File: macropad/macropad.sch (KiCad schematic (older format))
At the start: 0 parts

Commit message: added new component lib
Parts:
- added C1, C2: 20p, symbol Device:C_Small
- added R1: 10K, symbol Device:R
- added SW1: RESET, symbol keyboard_parts:SW_PUSH
- added SW2: BOOT, symbol keyboard_parts:SW_PUSH
- added U1: ATmega328-PU, Package_DIP:DIP-28_W7.62mm, symbol MCU_Microchip_ATmega:ATmega328-PU
- added Y1: 16MHz, symbol Device:Crystal
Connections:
- new net: R1.2, SW1.1, U1.1 (~RESET~/PC6)
- new net: C1.1, U1.10 (XTAL2/PB7), Y1.2
- new net: SW2.1, U1.11 (PD5)
- new net: C2.1, U1.9 (XTAL1/PB6), Y1.1
- new net +5V: C1.2, C2.2, SW1.2, SW2.2, U1.22 (GND), U1.8 (GND)
- new net VCC: R1.1, U1.20 (AVCC), U1.7 (VCC)
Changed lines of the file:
@@
 EESchema Schematic File Version 4
+LIBS:macropad-cache
 EELAYER 26 0
 EELAYER END
@@
 Comment4 ""
 $EndDescr
+$Comp
+L MCU_Microchip_ATmega:ATmega328-PU U1
+U 1 1 5CCD0C9A
+P 2200 5200
+F 0 "U1" H 1559 5246 50  0000 R CNN
+F 1 "ATmega328-PU" H 1559 5155 50  0000 R CNN
+F 2 "Package_DIP:DIP-28_W7.62mm" H 2200 5200 50  0001 C CIN
+F 3 "http://ww1.microchip.com/downloads/en/DeviceDoc/ATmega328_P%20AVR%20MCU%20with%20picoPower%20Technology%20Data%20Sheet%2040001984A.pdf" H 2200 5200 50  0001 C CNN
+	1    2200 5200
+	1    0    0    -1
+$EndComp
+$Comp
+L Device:Crystal Y1
+U 1 1 5CCD0E54
+P 3950 4450
+F 0 "Y1" V 3904 4581 50  0000 L CNN
+F 1 "16MHz" V 3995 4581 50  0000 L CNN
+F 2 "" H 3950 4450 50  0001 C CNN
+F 3 "~" H 3950 4450 50  0001 C CNN
+F 4 " X176-ND " H 3950 4450 50  0001 C CNN "DPN"
+F 5 " ECS-160-20-4 " H 3950 4450 50  0001 C CNN "MPN"
+	1    3950 4450
+	0    1    1    0
+$EndComp
+Wire Wire Line
+	2800 4600 3650 4600
+Wire Wire Line
+	3650 4600 3650 4200
+Wire Wire Line
+	3650 4200 3950 4200
+Wire Wire Line
+	3950 4200 3950 4300
+Wire Wire Line
+	2800 4700 3950 4700
+Wire Wire Line
+	3950 4700 3950 4600
+$Comp
+L Device:C_Small C2
+U 1 1 5CCD1142
+P 4250 4900
+F 0 "C2" H 4342 4946 50  0000 L CNN
+F 1 "20p" H 4342 4855 50  0000 L CNN
+F 2 "" H 4250 4900 50  0001 C CNN
+F 3 "~" H 4250 4900 50  0001 C CNN
+F 4 "478-7724-ND" H 4250 4900 50  0001 C CNN "DPN"
+F 5 "SR151A200JAR" H 4250 4900 50  0001 C CNN "MPN"
+	1    4250 4900
+	1    0    0    -1
+$EndComp
+$Comp
+L Device:C_Small C1
+U 1 1 5CCD117E
+P 3950 4900
+F 0 "C1" H 4042 4946 50  0000 L CNN
+F 1 "20p" H 4042 4855 50  0000 L CNN
+F 2 "" H 3950 4900 50  0001 C CNN
+F 3 "~" H 3950 4900 50  0001 C CNN
+F 4 "SR151A200JAR" H 3950 4900 50  0001 C CNN "MPN"
+F 5 "478-7724-ND" H 3950 4900 50  0001 C CNN "DPN"
+	1    3950 4900
+	1    0    0    -1
+$EndComp
+Wire Wire Line
+	3950 4800 3950 4700
+Connection ~ 3950 4700
+Wire Wire Line
+	4250 4800 4250 4200
+Wire Wire Line
+	4250 4200 3950 4200
+Connection ~ 3950 4200
+$Comp
+L keyboard_parts:GND #PWR?
+U 1 1 5CCD12BD
+P 4250 5250
+F 0 "#PWR?" H 4250 5300 20  0001 C CNN
+F 1 "GND" H 4250 5309 30  0000 C CNN
+F 2 "" H 4250 5250 60  0000 C CNN
+F 3 "" H 4250 5250 60  0000 C CNN
+	1    4250 5250
+	1    0    0    -1
+$EndComp
+Wire Wire Line
+	4250 5000 4250 5100
+Wire Wire Line
+	3950 5000 3950 5100
+Wire Wire Line
+	3950 5100 4250 5100
+Connection ~ 4250 5100
+Wire Wire Line
+	4250 5100 4250 5250
+$Comp
+L power:VCC #PWR?
+U 1 1 5CCD1372
+P 2200 3300
+F 0 "#PWR?" H 2200 3150 50  0001 C CNN
+F 1 "VCC" H 2217 3473 50  0000 C CNN
+F 2 "" H 2200 3300 50  0001 C CNN
+F 3 "" H 2200 3300 50  0001 C CNN
+	1    2200 3300
+	1    0    0    -1
+$EndComp
+Wire Wire Line
+	2200 3700 2200 3450
+Wire Wire Line
+	2300 3700 2300 3450
+Wire Wire Line
+	2300 3450 2200 3450
+Connection ~ 2200 3450
+Wire Wire Line
+	2200 3450 2200 3300
+$Comp
+L keyboard_parts:GND #PWR?
+U 1 1 5CCD165F
+P 2200 6950
+F 0 "#PWR?" H 2200 7000 20  0001 C CNN
+F 1 "GND" H 2200 7009 30  0000 C CNN
+F 2 "" H 2200 6950 60  0000 C CNN
+F 3 "" H 2200 6950 60  0000 C CNN
+	1    2200 6950
+	1    0    0    -1
+$EndComp
+Wire Wire Line
+	2200 6700 2200 6950
+$Comp
+L keyboard_parts:SW_PUSH SW1
+U 1 1 5CCD150D
+P 3950 5700
+F 0 "SW1" H 3950 5955 50  0000 C CNN
+F 1 "RESET" H 3950 5864 50  0000 C CNN
+F 2 "" H 3950 5700 60  0000 C CNN
+F 3 "" H 3950 5700 60  0000 C CNN
+	1    3950 5700
+	1    0    0    -1
+$EndComp
+$Comp
+L keyboard_parts:SW_PUSH SW2
+U 1 1 5CCD1582
+P 3950 6200
+F 0 "SW2" H 3950 6455 50  0000 C CNN
+F 1 "BOOT" H 3950 6364 50  0000 C CNN
+F 2 "" H 3950 6200 60  0000 C CNN
+F 3 "" H 3950 6200 60  0000 C CNN
+	1    3950 6200
+	1    0    0    -1
+$EndComp
+$Comp
+L Device:R R1
+U 1 1 5CCD16E0
+P 3450 5350
+F 0 "R1" H 3520 5396 50  0000 L CNN
+F 1 "10K" H 3520 5305 50  0000 L CNN
+F 2 "" V 3380 5350 50  0001 C CNN
+F 3 "~" H 3450 5350 50  0001 C CNN
+	1    3450 5350
+	1    0    0    -1
+$EndComp
+$Comp
+L power:VCC #PWR?
+U 1 1 5CCD183E
+P 3450 5050
+F 0 "#PWR?" H 3450 4900 50  0001 C CNN
+F 1 "VCC" H 3467 5223 50  0000 C CNN
+F 2 "" H 3450 5050 50  0001 C CNN
+F 3 "" H 3450 5050 50  0001 C CNN
+	1    3450 5050
+	1    0    0    -1
+$EndComp
+Wire Wire Line
+	2800 5500 3100 5500
+Wire Wire Line
+	3100 5500 3100 5700
+Wire Wire Line
+	3100 5700 3450 5700
+Wire Wire Line
+	3450 5500 3450 5700
+Connection ~ 3450 5700
+Wire Wire Line
+	3450 5700 3650 5700
+Wire Wire Line
+	3450 5200 3450 5050
+Wire Wire Line
+	2800 6200 3650 6200
+$Comp
+L keyboard_parts:GND #PWR?
+U 1 1 5CCD26A4
+P 4400 6450
+F 0 "#PWR?" H 4400 6500 20  0001 C CNN
+F 1 "GND" H 4400 6509 30  0000 C CNN
+F 2 "" H 4400 6450 60  0000 C CNN
+F 3 "" H 4400 6450 60  0000 C CNN
+	1    4400 6450
+	1    0    0    -1
+$EndComp
+Wire Wire Line
+	4250 5700 4400 5700
+Wire Wire Line
+	4400 5700 4400 6200
+Wire Wire Line
+	4250 6200 4400 6200
+Connection ~ 4400 6200
+Wire Wire Line
+	4400 6200 4400 6450
 $EndSCHEMATC

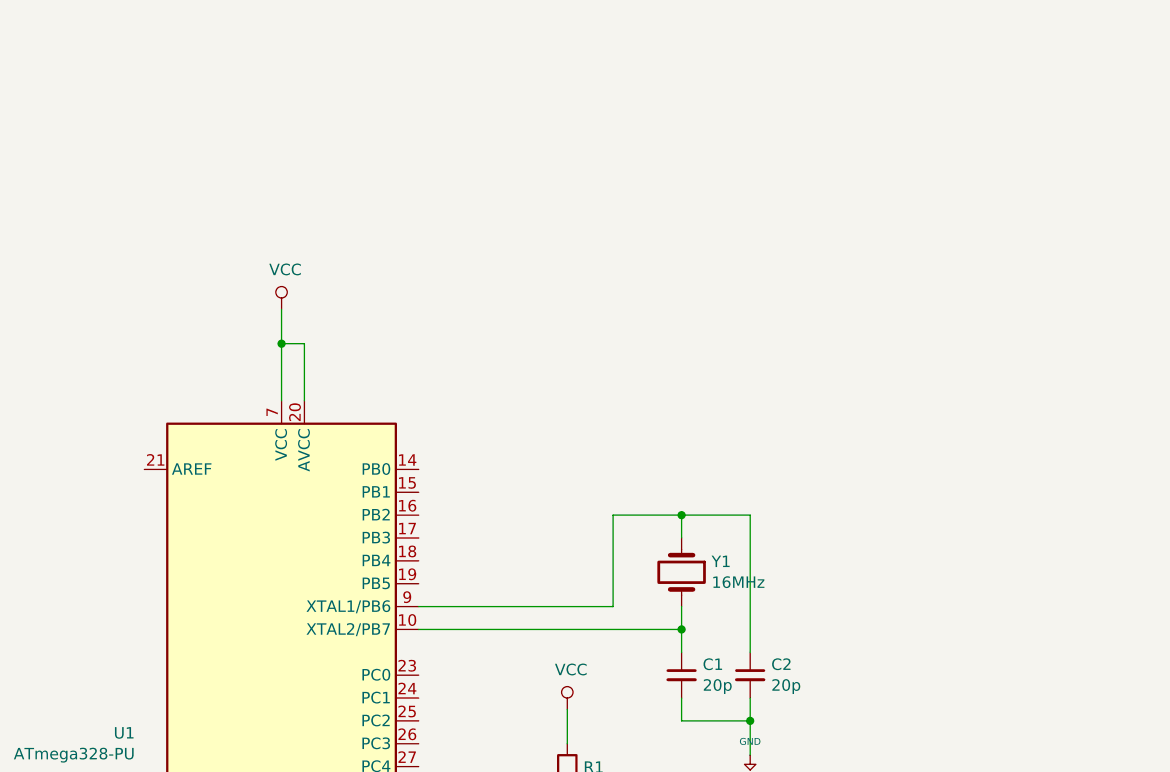
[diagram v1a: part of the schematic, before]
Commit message: added more components to pcb
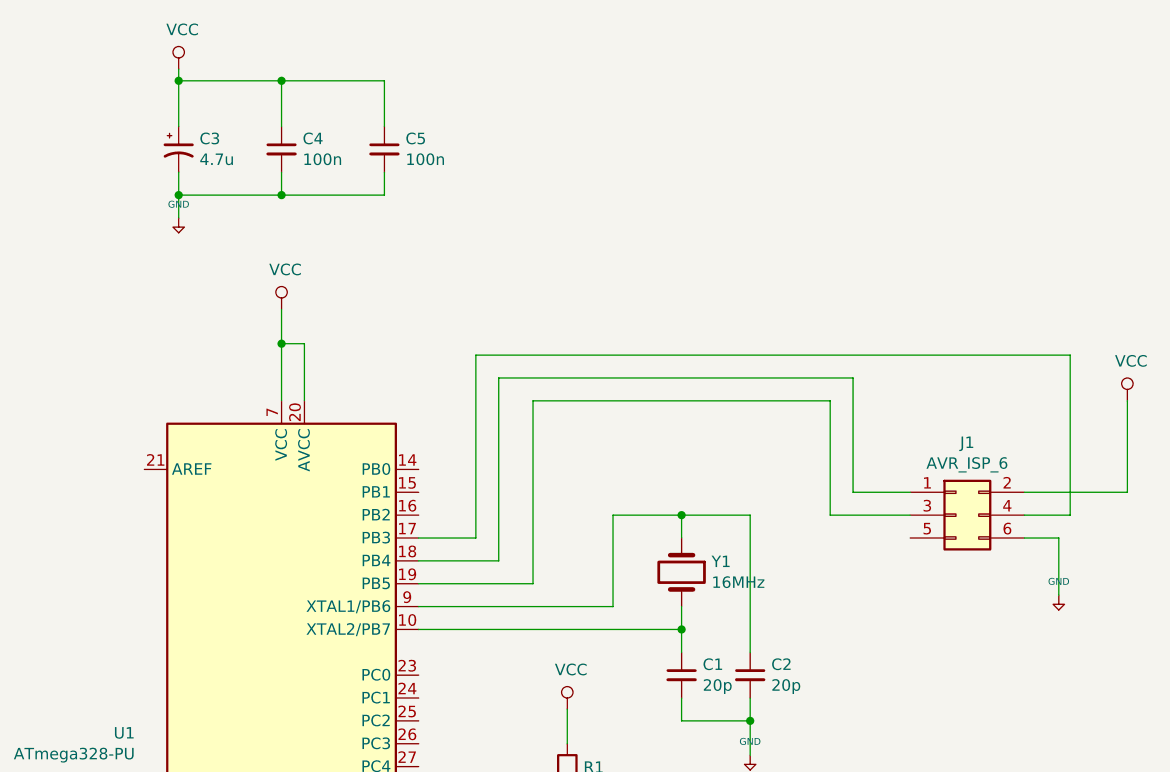
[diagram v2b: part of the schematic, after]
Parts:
- added C3: 4.7u, symbol Device:CP1_Small
- added C4, C5: 100n, symbol Device:C_Small
- added J1: AVR_ISP_6, symbol Connector_Generic:Conn_02x03_Odd_Even
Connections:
- net +5V: now also C3.2, C4.2, C5.2, J1.6 (Pin_6)
- net VCC: now also C3.1, C4.1, C5.1, J1.2 (Pin_2)
- net at U1.17 (PB3): now also J1.4 (Pin_4)
- net at U1.18 (PB4): now also J1.1 (Pin_1)
- net at U1.19 (PB5): now also J1.3 (Pin_3)
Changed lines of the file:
@@
 Wire Wire Line
 	4400 6200 4400 6450
+$Comp
+L Connector_Generic:Conn_02x03_Odd_Even J1
+U 1 1 5CCD1A31
+P 5150 4200
+F 0 "J1" H 5200 4517 50  0000 C CNN
+F 1 "AVR_ISP_6" H 5200 4426 50  0000 C CNN
+F 2 "" H 5150 4200 50  0001 C CNN
+F 3 "~" H 5150 4200 50  0001 C CNN
+	1    5150 4200
+	1    0    0    -1
+$EndComp
+Wire Wire Line
+	2800 4400 3150 4400
+Wire Wire Line
+	3150 4400 3150 3600
+Wire Wire Line
+	3150 3600 4700 3600
+Wire Wire Line
+	4700 3600 4700 4100
+Wire Wire Line
+	4700 4100 4950 4100
+Wire Wire Line
+	2800 4500 3300 4500
+Wire Wire Line
+	3300 4500 3300 3700
+Wire Wire Line
+	3300 3700 4600 3700
+Wire Wire Line
+	4600 3700 4600 4200
+Wire Wire Line
+	4600 4200 4950 4200
+Wire Wire Line
+	2800 4300 3050 4300
+Wire Wire Line
+	3050 4300 3050 3500
+Wire Wire Line
+	3050 3500 5650 3500
+Wire Wire Line
+	5650 3500 5650 4200
+Wire Wire Line
+	5650 4200 5450 4200
+$Comp
+L power:VCC #PWR?
+U 1 1 5CCD2F07
+P 5900 3700
+F 0 "#PWR?" H 5900 3550 50  0001 C CNN
+F 1 "VCC" H 5917 3873 50  0000 C CNN
+F 2 "" H 5900 3700 50  0001 C CNN
+F 3 "" H 5900 3700 50  0001 C CNN
+	1    5900 3700
+	1    0    0    -1
+$EndComp
+Wire Wire Line
+	5450 4100 5900 4100
+Wire Wire Line
+	5900 4100 5900 3700
+$Comp
+L keyboard_parts:GND #PWR?
+U 1 1 5CCD3889
+P 5600 4550
+F 0 "#PWR?" H 5600 4600 20  0001 C CNN
+F 1 "GND" H 5600 4609 30  0000 C CNN
+F 2 "" H 5600 4550 60  0000 C CNN
+F 3 "" H 5600 4550 60  0000 C CNN
+	1    5600 4550
+	1    0    0    -1
+$EndComp
+Wire Wire Line
+	5450 4300 5600 4300
+Wire Wire Line
+	5600 4300 5600 4550
+$Comp
+L Device:CP1_Small C3
+U 1 1 5CCD43B1
+P 1750 2600
+F 0 "C3" H 1841 2646 50  0000 L CNN
+F 1 "4.7u" H 1841 2555 50  0000 L CNN
+F 2 "" H 1750 2600 50  0001 C CNN
+F 3 "~" H 1750 2600 50  0001 C CNN
+	1    1750 2600
+	1    0    0    -1
+$EndComp
+$Comp
+L Device:C_Small C4
+U 1 1 5CCD4462
+P 2200 2600
+F 0 "C4" H 2292 2646 50  0000 L CNN
+F 1 "100n" H 2292 2555 50  0000 L CNN
+F 2 "" H 2200 2600 50  0001 C CNN
+F 3 "~" H 2200 2600 50  0001 C CNN
+	1    2200 2600
+	1    0    0    -1
+$EndComp
+$Comp
+L Device:C_Small C5
+U 1 1 5CCD44D9
+P 2650 2600
+F 0 "C5" H 2742 2646 50  0000 L CNN
+F 1 "100n" H 2742 2555 50  0000 L CNN
+F 2 "" H 2650 2600 50  0001 C CNN
+F 3 "~" H 2650 2600 50  0001 C CNN
+	1    2650 2600
+	1    0    0    -1
+$EndComp
+$Comp
+L keyboard_parts:GND #PWR?
+U 1 1 5CCD456B
+P 1750 2900
+F 0 "#PWR?" H 1750 2950 20  0001 C CNN
+F 1 "GND" H 1750 2959 30  0000 C CNN
+F 2 "" H 1750 2900 60  0000 C CNN
+F 3 "" H 1750 2900 60  0000 C CNN
+	1    1750 2900
+	1    0    0    -1
+$EndComp
+$Comp
+L power:VCC #PWR?
+U 1 1 5CCD45F4
+P 1750 2250
+F 0 "#PWR?" H 1750 2100 50  0001 C CNN
+F 1 "VCC" H 1767 2423 50  0000 C CNN
+F 2 "" H 1750 2250 50  0001 C CNN
+F 3 "" H 1750 2250 50  0001 C CNN
+	1    1750 2250
+	1    0    0    -1
+$EndComp
+Wire Wire Line
+	1750 2500 1750 2300
+Wire Wire Line
+	2200 2500 2200 2300
+Wire Wire Line
+	2200 2300 1750 2300
+Connection ~ 1750 2300
+Wire Wire Line
+	1750 2300 1750 2250
+Wire Wire Line
+	2650 2500 2650 2300
+Wire Wire Line
+	2650 2300 2200 2300
+Connection ~ 2200 2300
+Wire Wire Line
+	1750 2700 1750 2800
+Wire Wire Line
+	2200 2700 2200 2800
+Wire Wire Line
+	2200 2800 1750 2800
+Connection ~ 1750 2800
+Wire Wire Line
+	1750 2800 1750 2900
+Wire Wire Line
+	2650 2700 2650 2800
+Wire Wire Line
+	2650 2800 2200 2800
+Connection ~ 2200 2800
 $EndSCHEMATC

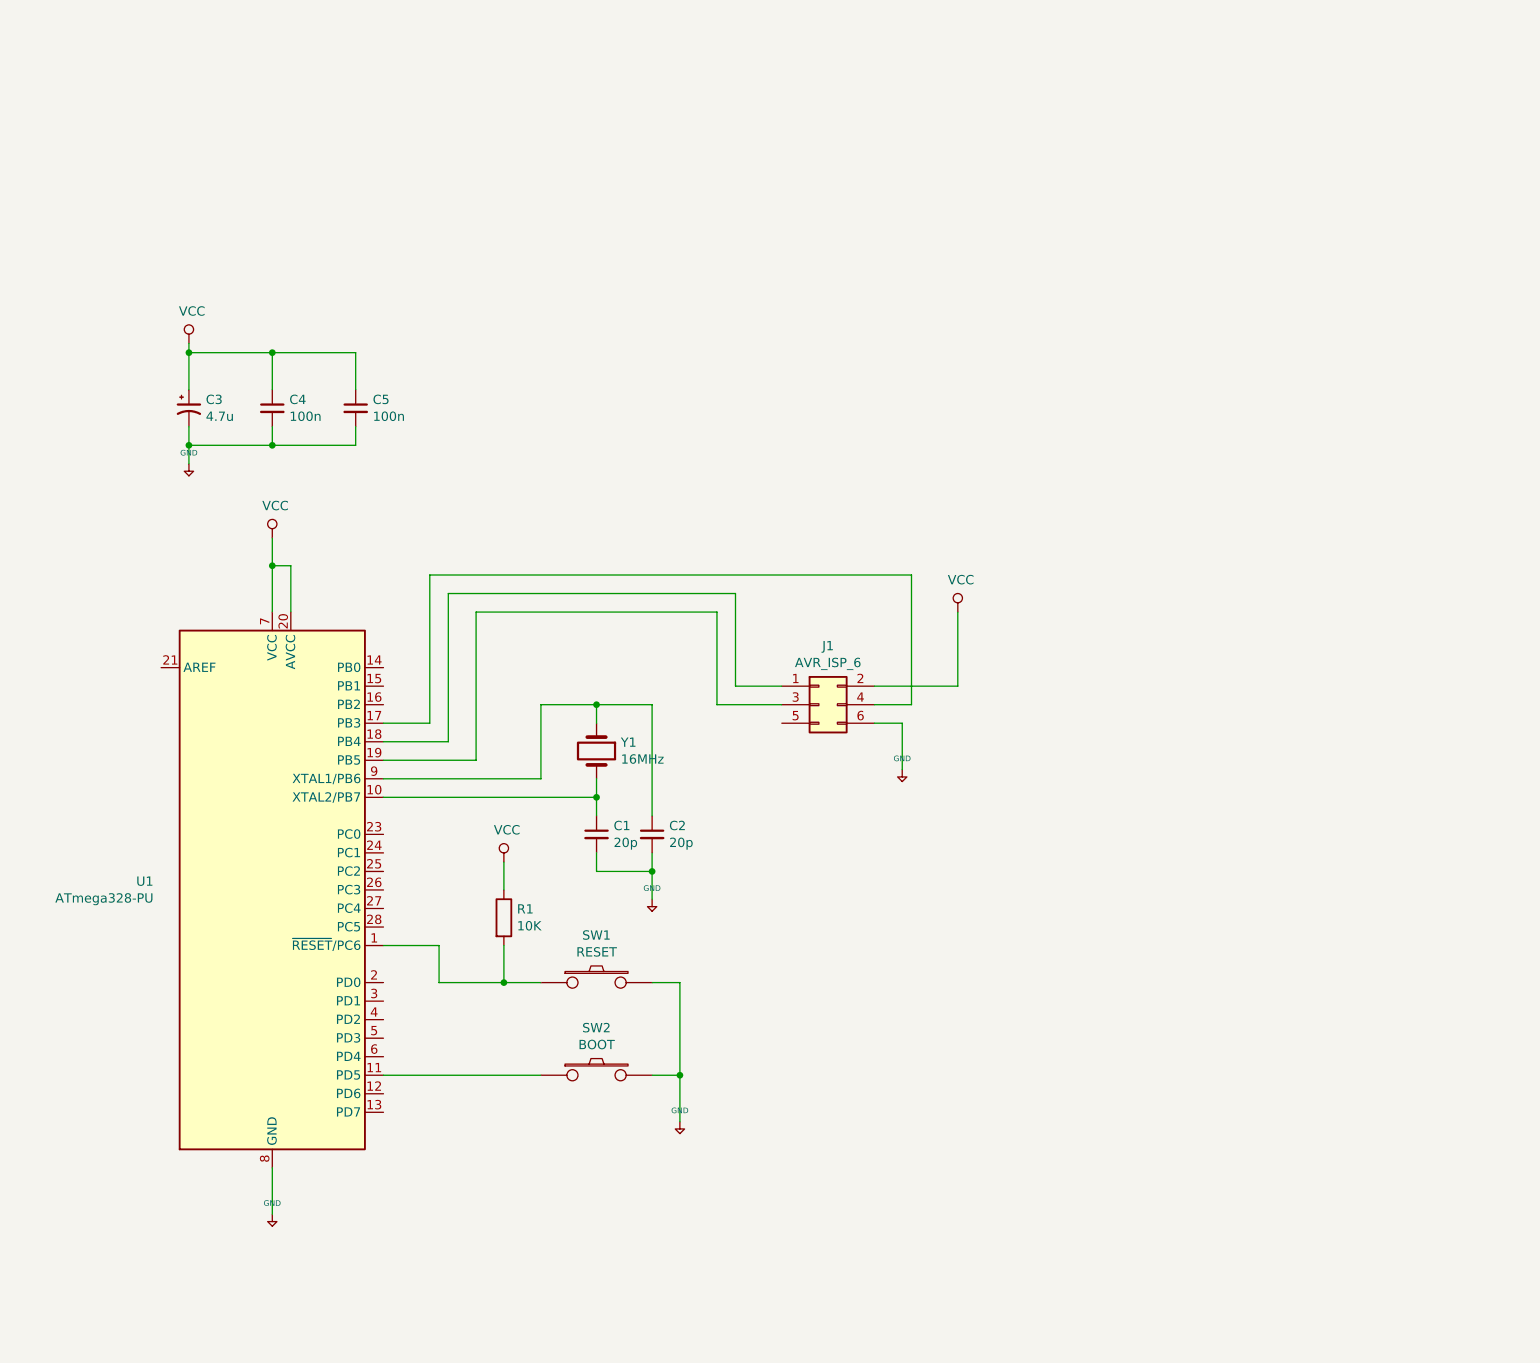
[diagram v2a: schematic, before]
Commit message: added usb port and i2c port to the schematic
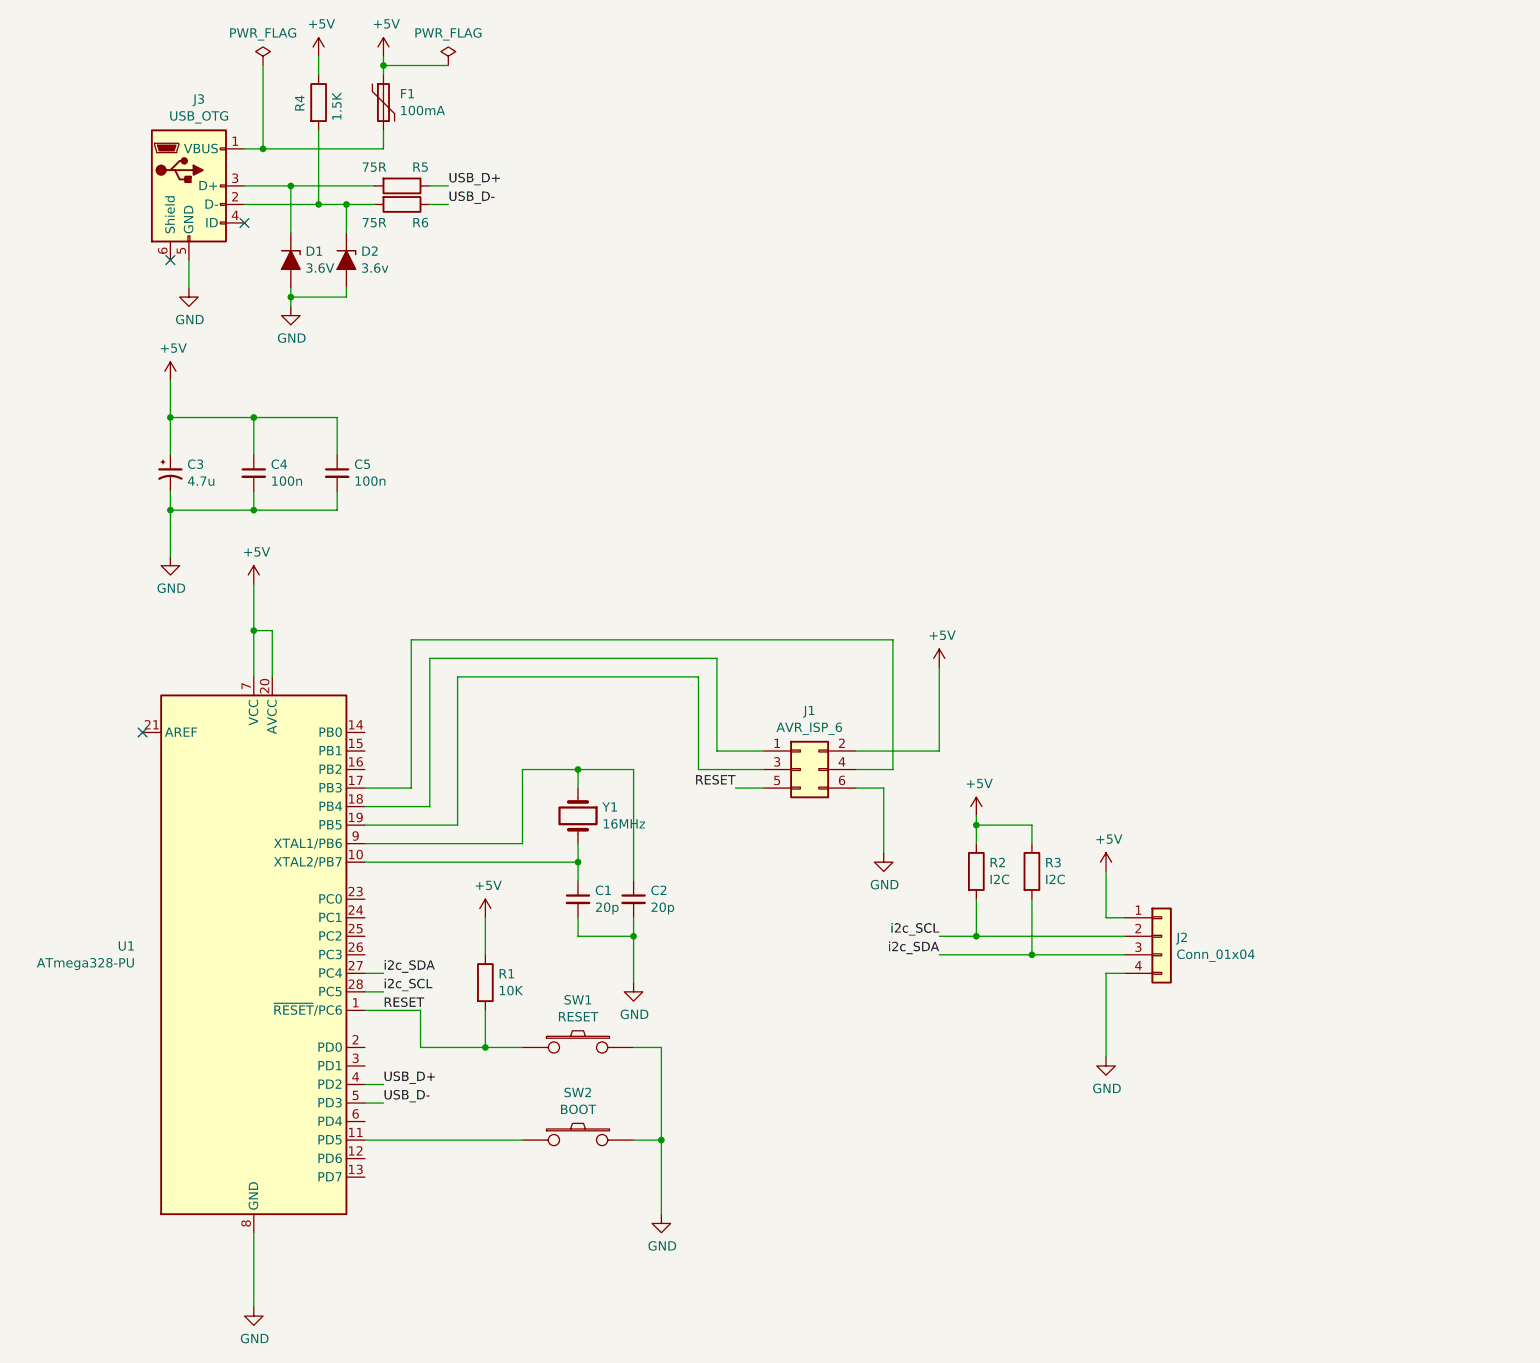
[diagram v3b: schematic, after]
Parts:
- added D1: 3.6V, symbol Device:D_Zener_ALT
- added D2: 3.6v, symbol Device:D_Zener_ALT
- added F1: 100mA, symbol Device:Polyfuse
- added J2: Conn_01x04, symbol Connector_Generic:Conn_01x04
- added J3: USB_OTG, symbol Connector:USB_OTG
- added R2, R3: I2C, symbol Device:R
- added R4: 1.5K, symbol Device:R
- added R5, R6: 75R, symbol Device:R
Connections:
- net VCC is gone; now on net +5V: C3.1, C4.1, C5.1, J1.2 (Pin_2), R1.1, U1.20 (AVCC), U1.7 (VCC)
- net +5V: now also F1.1, J2.1 (Pin_1), R2.1, R3.1, R4.1; no longer C1.2, C2.2, C3.2, C4.2, C5.2, J1.6 (Pin_6), SW1.2, SW2.2, U1.22 (GND), U1.8 (GND)
- net RESET: now reaches R1.2, SW1.1, U1.1 (~RESET~/PC6)
- net RESET: now also J1.5 (Pin_5)
- net i2c_SDA: now reaches U1.27 (PC4)
- net i2c_SDA: now also J2.3 (Pin_3), R3.2
- net i2c_SCL: now reaches U1.28 (PC5)
- net i2c_SCL: now also J2.2 (Pin_2), R2.2
- net USB_D+: now reaches U1.4 (PD2)
- net USB_D+: now also R5.1
- net USB_D-: now reaches U1.5 (PD3)
- net USB_D-: now also R6.1
- new net: D2.1 (K), J3.2 (D-), R4.2, R6.2
- new net: D1.1 (K), J3.3 (D+), R5.2
- new net: F1.2, J3.1 (VBUS)
- new net GND: C1.2, C2.2, C3.2, C4.2, C5.2, D1.2 (A), D2.2 (A), J1.6 (Pin_6), J2.4 (Pin_4), J3.5 (GND), SW1.2, SW2.2, U1.22 (GND), U1.8 (GND)
- no-connect marks 0 -> 3
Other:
- moved on the sheet: C1, C2, C3, C4, C5, J1, R1, SW1, SW2, U1, Y1
